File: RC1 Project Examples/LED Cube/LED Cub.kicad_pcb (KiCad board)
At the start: 2 copper layers, 99.1 x 69.2 mm, 8 parts, among them J1 Signals, J5 Port A, J6 Port B, J7 PWR1, J8 PWR2

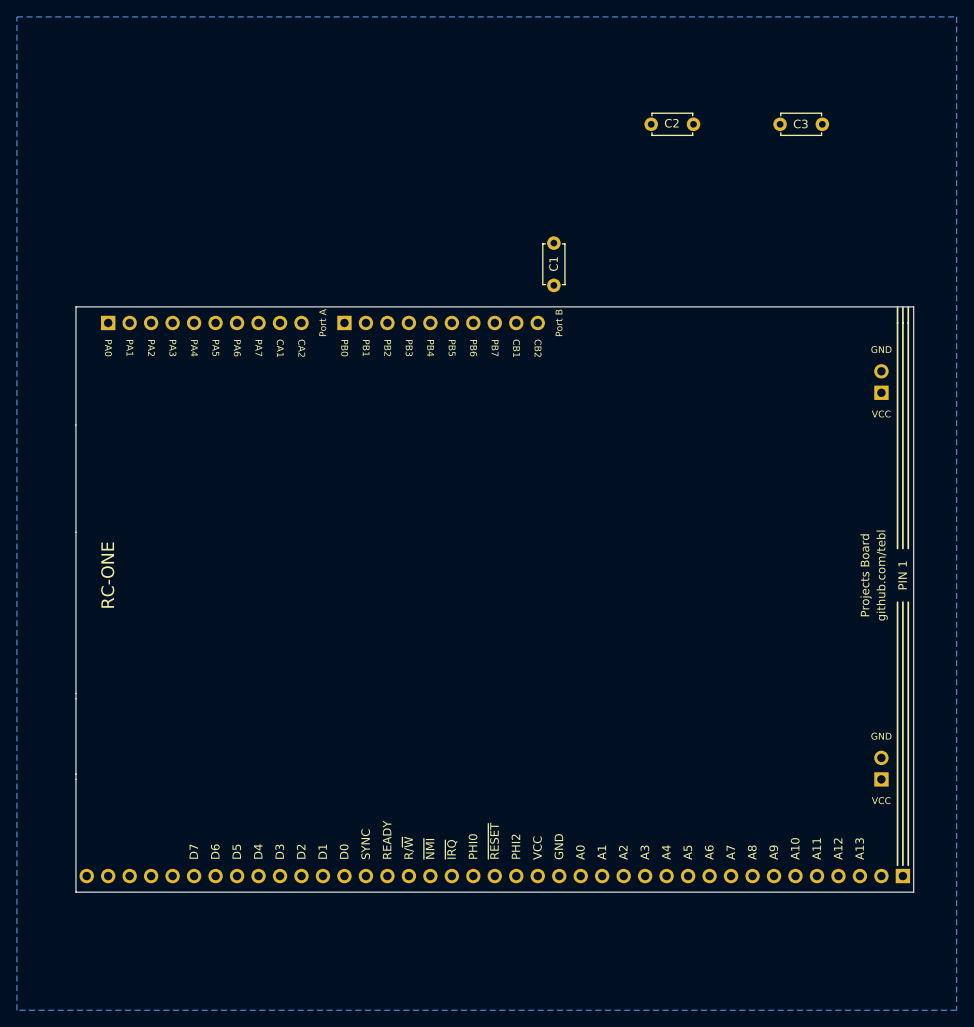
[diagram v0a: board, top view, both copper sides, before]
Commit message: LED Cube schematic updated
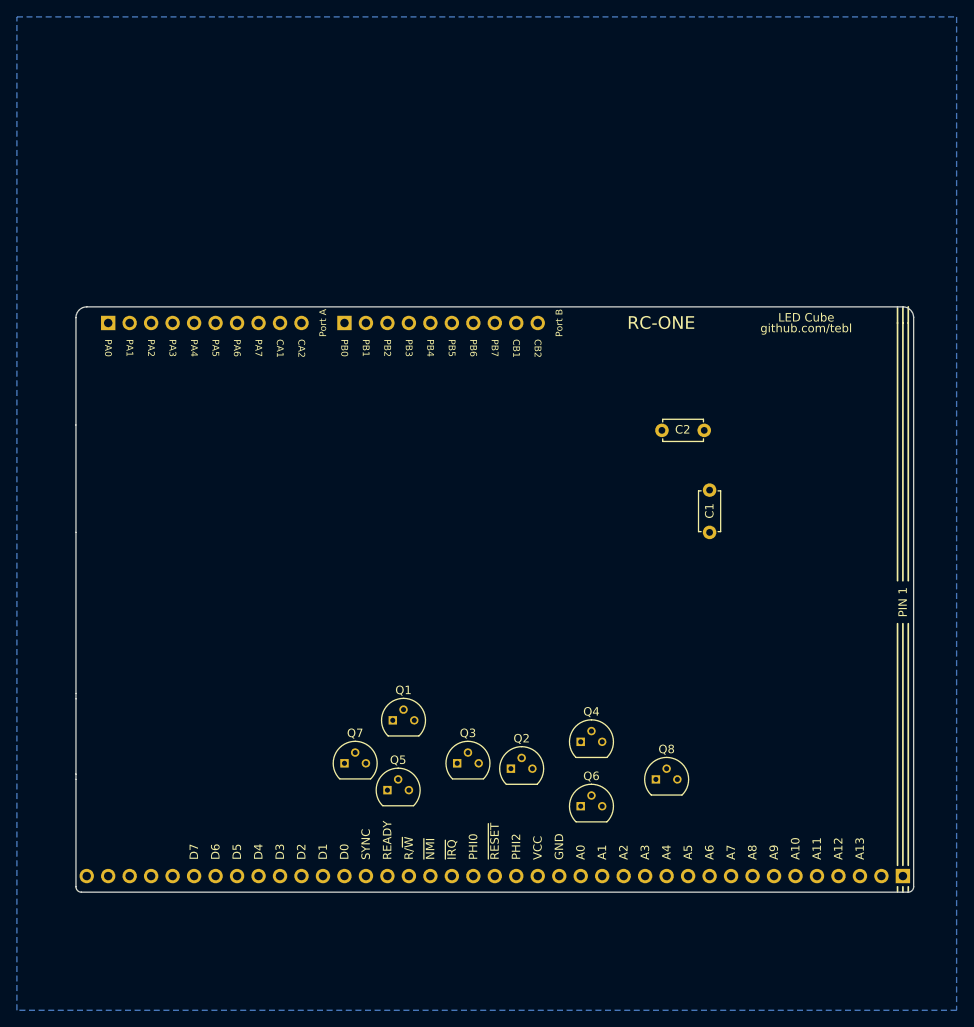
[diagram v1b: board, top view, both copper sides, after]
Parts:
- removed C3: 100nF, Capacitors_THT:C_Disc_D4.7mm_W2.5mm_P5.00mm
- removed J7: PWR1, Pin_Headers:Pin_Header_Straight_1x02_Pitch2.54mm
- removed J8: PWR2, Pin_Headers:Pin_Header_Straight_1x02_Pitch2.54mm
- added Q1: PN2222A, TO_SOT_Packages_THT:TO-92_Molded_Narrow, F.Cu at (137.8, 127.0)
- added Q2: PN2222A, TO_SOT_Packages_THT:TO-92_Molded_Narrow, F.Cu at (151.8, 132.7)
- added Q3: PN2222A, TO_SOT_Packages_THT:TO-92_Molded_Narrow, F.Cu at (145.4, 132.1)
- added Q4: PN2222A, TO_SOT_Packages_THT:TO-92_Molded_Narrow, F.Cu at (160.0, 129.5)
- added Q5: PN2222A, TO_SOT_Packages_THT:TO-92_Molded_Narrow, F.Cu at (137.2, 135.3)
- added Q6: PN2222A, TO_SOT_Packages_THT:TO-92_Molded_Narrow, F.Cu at (160.0, 137.2)
- added Q7: PN2222A, TO_SOT_Packages_THT:TO-92_Molded_Narrow, F.Cu at (132.1, 132.1)
- added Q8: PN2222A, TO_SOT_Packages_THT:TO-92_Molded_Narrow, F.Cu at (168.9, 134.0)
- moved C2 36.2 mm to (174.6, 92.7)
- moved C1 34.5 mm to (175.3, 104.8)
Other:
- outline, holes or cut-outs redrawn
- board text added: "LED Cube"
- board text removed: "Projects Board"

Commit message: Layout done
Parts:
- removed Q5, Q6, Q7, Q8: PN2222A, TO_SOT_Packages_THT:TO-92_Molded_Narrow
- added A1: LED_Cube_4x4, led_cube:LED_Cube_4x4, F.Cu at (149.2, 115.6)
- added M1: Mounting, mounting:1pin, F.Cu at (104.1, 140.3)
- added M2: Mounting, mounting:1pin, F.Cu at (195.6, 140.3)
- added M3: Mounting, mounting:1pin, F.Cu at (195.6, 81.3)
- added R1: 100, Resistors_THT:R_Axial_DIN0207_L6.3mm_D2.5mm_P10.16mm_Horizontal, F.Cu at (104.8, 121.9)
- added R10: 100, Resistors_THT:R_Axial_DIN0207_L6.3mm_D2.5mm_P10.16mm_Horizontal, F.Cu at (158.1, 93.3)
- added R11: 100, Resistors_THT:R_Axial_DIN0207_L6.3mm_D2.5mm_P10.16mm_Horizontal, F.Cu at (172.1, 93.3)
- added R12: 100, Resistors_THT:R_Axial_DIN0207_L6.3mm_D2.5mm_P10.16mm_Horizontal, F.Cu at (186.1, 93.3)
- added R13: 1k, Resistors_THT:R_Axial_DIN0207_L6.3mm_D2.5mm_P10.16mm_Horizontal, F.Cu at (132.7, 141.6)
- added R14: 1k, Resistors_THT:R_Axial_DIN0207_L6.3mm_D2.5mm_P10.16mm_Horizontal, F.Cu at (132.7, 137.2)
- added R15: 100, Resistors_THT:R_Axial_DIN0207_L6.3mm_D2.5mm_P10.16mm_Horizontal, F.Cu at (144.1, 97.2)
- added R16: 100, Resistors_THT:R_Axial_DIN0207_L6.3mm_D2.5mm_P10.16mm_Horizontal, F.Cu at (158.1, 97.2)
- added R17: 100, Resistors_THT:R_Axial_DIN0207_L6.3mm_D2.5mm_P10.16mm_Horizontal, F.Cu at (172.1, 97.2)
- added R18: 100, Resistors_THT:R_Axial_DIN0207_L6.3mm_D2.5mm_P10.16mm_Horizontal, F.Cu at (186.1, 97.2)
- added R19: 100, Resistors_THT:R_Axial_DIN0207_L6.3mm_D2.5mm_P10.16mm_Horizontal, F.Cu at (144.1, 123.8)
- added R2: 100, Resistors_THT:R_Axial_DIN0207_L6.3mm_D2.5mm_P10.16mm_Horizontal, F.Cu at (111.8, 121.9)
- added R20: 100, Resistors_THT:R_Axial_DIN0207_L6.3mm_D2.5mm_P10.16mm_Horizontal, F.Cu at (158.1, 123.8)
- added R21: 100, Resistors_THT:R_Axial_DIN0207_L6.3mm_D2.5mm_P10.16mm_Horizontal, F.Cu at (172.1, 123.8)
- added R22: 100, Resistors_THT:R_Axial_DIN0207_L6.3mm_D2.5mm_P10.16mm_Horizontal, F.Cu at (186.1, 123.8)
- added R23: 100, Resistors_THT:R_Axial_DIN0207_L6.3mm_D2.5mm_P10.16mm_Horizontal, F.Cu at (144.1, 127.6)
- added R24: 100, Resistors_THT:R_Axial_DIN0207_L6.3mm_D2.5mm_P10.16mm_Horizontal, F.Cu at (158.1, 127.6)
- added R25: 100, Resistors_THT:R_Axial_DIN0207_L6.3mm_D2.5mm_P10.16mm_Horizontal, F.Cu at (172.1, 127.6)
- added R26: 100, Resistors_THT:R_Axial_DIN0207_L6.3mm_D2.5mm_P10.16mm_Horizontal, F.Cu at (186.1, 127.6)
- added R3: 100, Resistors_THT:R_Axial_DIN0207_L6.3mm_D2.5mm_P10.16mm_Horizontal, F.Cu at (118.7, 121.9)
- added R4: 100, Resistors_THT:R_Axial_DIN0207_L6.3mm_D2.5mm_P10.16mm_Horizontal, F.Cu at (125.7, 121.9)
- added R5: 100, Resistors_THT:R_Axial_DIN0207_L6.3mm_D2.5mm_P10.16mm_Horizontal, F.Cu at (114.9, 121.9)
- added R6: 100, Resistors_THT:R_Axial_DIN0207_L6.3mm_D2.5mm_P10.16mm_Horizontal, F.Cu at (121.9, 121.9)
- added R7: 100, Resistors_THT:R_Axial_DIN0207_L6.3mm_D2.5mm_P10.16mm_Horizontal, F.Cu at (128.9, 121.9)
- added R8: 100, Resistors_THT:R_Axial_DIN0207_L6.3mm_D2.5mm_P10.16mm_Horizontal, F.Cu at (144.1, 93.3)
- added R9: 100, Resistors_THT:R_Axial_DIN0207_L6.3mm_D2.5mm_P10.16mm_Horizontal, F.Cu at (108.0, 121.9)
- added SW1: SW_Push, Buttons_Switches_THT:SW_PUSH_6mm, F.Cu at (110.5, 137.2)
- added SW2: SW_Push, Buttons_Switches_THT:SW_PUSH_6mm, F.Cu at (121.9, 137.2)
- added U1: 74LS374, Housings_DIP:DIP-20_W7.62mm_Socket_LongPads, F.Cu at (106.0, 95.9)
- added U2: 74LS374, Housings_DIP:DIP-20_W7.62mm_Socket_LongPads, F.Cu at (106.0, 111.1)
- moved C1 73.0 mm to (102.2, 104.8), turned to 270 degrees
- moved C2 72.5 mm to (102.2, 89.5), turned to 270 degrees
- moved Q2 42.2 mm to (112.4, 117.5)
- moved Q4 35.8 mm to (126.4, 117.5)
- moved Q1 33.8 mm to (105.4, 117.5)
- moved Q3 29.9 mm to (119.4, 117.5)
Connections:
- J5 pad 1: (no net) -> /PA0
- J5 pad 2: (no net) -> /PA1
- J5 pad 3: (no net) -> /PA2
- J5 pad 4: (no net) -> /PA3
- J5 pad 5: (no net) -> /PA4
- J5 pad 6: (no net) -> /PA5
- J5 pad 7: (no net) -> /PA6
- J5 pad 8: (no net) -> /PA7
- J6 pad 1: (no net) -> /PB0
- J6 pad 2: (no net) -> /PB1
- J6 pad 3: (no net) -> /PB2
- J6 pad 4: (no net) -> /PB3
- J6 pad 5: (no net) -> /PB4
- J6 pad 6: (no net) -> /PB5
- J6 pad 7: (no net) -> /PB6
- J6 pad 8: (no net) -> /PB7
- Q1 pad 2: (no net) -> Net-(Q1-Pad2)
- Q1 pad 3: Net-(A1-Pad16) -> Net-(A1-Pad17)
- Q2 pad 2: (no net) -> Net-(Q2-Pad2)
- Q2 pad 3: Net-(A1-Pad16) -> Net-(A1-Pad18)
- Q3 pad 2: (no net) -> Net-(Q3-Pad2)
- Q3 pad 3: Net-(A1-Pad17) -> Net-(A1-Pad19)
- Q4 pad 2: (no net) -> Net-(Q4-Pad2)
- Q4 pad 3: Net-(A1-Pad17) -> Net-(A1-Pad20)
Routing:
- net VCC: track 0.00 -> 126.9 mm
- net Net-(R26-Pad2): track 0.00 -> 109.8 mm, vias 0 -> 1
- net Net-(R18-Pad2): track 0.00 -> 107.3 mm, vias 0 -> 1
- net /PB7: track 0.00 -> 100.0 mm, vias 0 -> 2
- net Net-(R25-Pad2): track 0.00 -> 89.0 mm, vias 0 -> 2
- net Net-(R17-Pad2): track 0.00 -> 85.9 mm, vias 0 -> 1
- net Net-(R22-Pad2): track 0.00 -> 83.8 mm, vias 0 -> 3
- net /PB2: track 0.00 -> 82.5 mm
- net /PB6: track 0.00 -> 79.1 mm, vias 0 -> 2
- net Net-(R21-Pad2): track 0.00 -> 78.7 mm, vias 0 -> 3
- net /PB3: track 0.00 -> 77.4 mm
- net Net-(R12-Pad2): track 0.00 -> 75.3 mm, vias 0 -> 2
- net Net-(R24-Pad2): track 0.00 -> 72.9 mm, vias 0 -> 2
- net /PB4: track 0.00 -> 71.8 mm
- net Net-(R20-Pad2): track 0.00 -> 68.5 mm, vias 0 -> 3
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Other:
- outline, holes or cut-outs redrawn
- board text removed: "A0"
- board text removed: "A1"
- board text removed: "A10"
- board text removed: "A11"
- board text removed: "A12"
- board text removed: "A13"
- board text removed: "A2"
- board text removed: "A3"
- board text removed: "A4"
- board text removed: "A5"
- board text removed: "A6"
- board text removed: "A7"
- board text removed: "A8"
- board text removed: "A9"
- board text removed: "CA1"
- board text removed: "CA2"
- board text removed: "CB1"
- board text removed: "CB2"
- board text removed: "D0"
- board text removed: "D1"
- board text removed: "D2"
- board text removed: "D3"
- board text removed: "D4"
- board text removed: "D5"
- board text removed: "D6"
- board text removed: "D7"
- board text removed: "GND"
- board text removed: "PHI0"
- board text removed: "PHI2"
- board text removed: "R/~W"
- board text removed: "READY"
- board text removed: "SYNC"
- board text removed: "VCC"
- board text removed: "~IRQ"
- board text removed: "~NMI"
- board text removed: "~RESET"
